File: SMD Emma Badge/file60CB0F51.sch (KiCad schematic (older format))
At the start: 10 parts, among them U401 74164, U402 74LS595, U403 74164, U404 74HC86, U405 74HC04

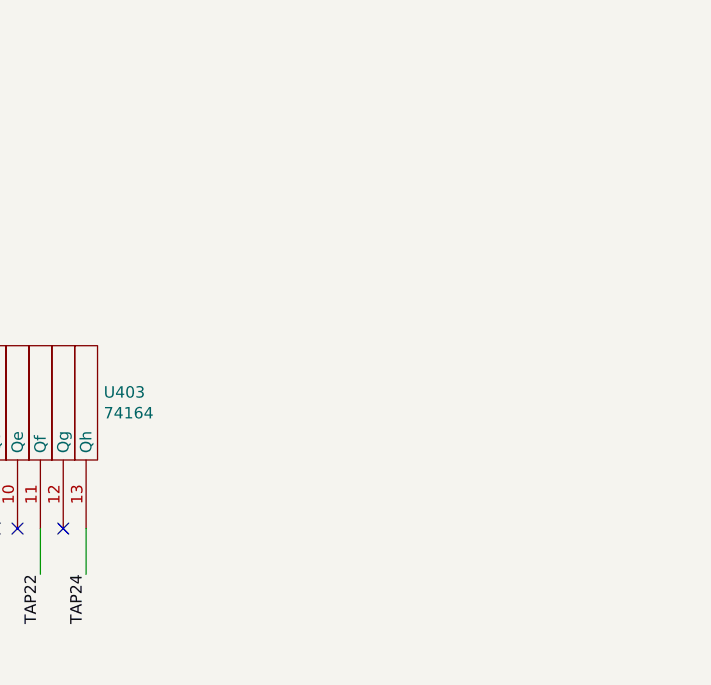
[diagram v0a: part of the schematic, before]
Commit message: Add power-on reset
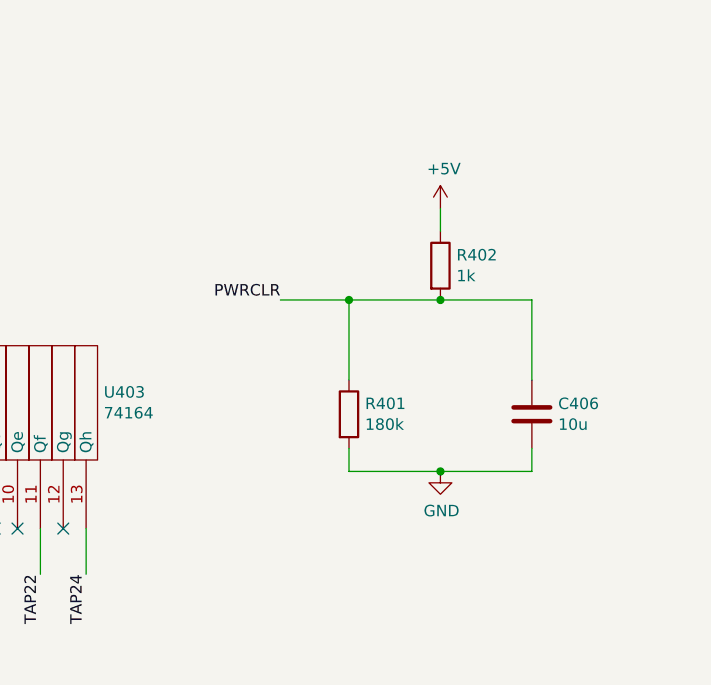
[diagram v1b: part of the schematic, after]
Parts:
- added C406: 10u, Capacitor_SMD:C_0603_1608Metric, symbol Device:C
- added R401: 180k, Resistor_SMD:R_0603_1608Metric, symbol Device:R
- added R402: 1k, Resistor_SMD:R_0603_1608Metric, symbol Device:R
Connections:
- net +5V: now also R402.1
- net GND: now also C406.2, R401.2
- net PWRCLR: now also C406.1, R401.1, R402.2
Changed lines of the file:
@@
 Connection ~ 2250 3200
 $Comp
-L power:+5V #PWR?
+L power:+5V #PWR0401
 U 1 1 60D3F3C4
 P 3150 6650
-F 0 "#PWR?" H 3150 6500 50  0001 C CNN
+F 0 "#PWR0401" H 3150 6500 50  0001 C CNN
 F 1 "+5V" V 3165 6778 50  0000 L CNN
 F 2 "" H 3150 6650 50  0001 C CNN
@@
 $EndComp
 $Comp
-L power:GND #PWR?
+L power:GND #PWR0402
 U 1 1 60D4000F
 P 3150 7650
-F 0 "#PWR?" H 3150 7400 50  0001 C CNN
+F 0 "#PWR0402" H 3150 7400 50  0001 C CNN
 F 1 "GND" V 3155 7522 50  0000 R CNN
 F 2 "" H 3150 7650 50  0001 C CNN
@@
 Connection ~ 3150 6650
 $Comp
-L power:GND #PWR?
+L power:GND #PWR0408
 U 1 1 60D48516
 P 10350 5900
-F 0 "#PWR?" H 10350 5650 50  0001 C CNN
+F 0 "#PWR0408" H 10350 5650 50  0001 C CNN
 F 1 "GND" H 10355 5727 50  0000 C CNN
 F 2 "" H 10350 5900 50  0001 C CNN
@@
 	10700 4650 10700 5100
 $Comp
-L power:+5V #PWR?
+L power:+5V #PWR0407
 U 1 1 60D50F40
 P 10250 4650
-F 0 "#PWR?" H 10250 4500 50  0001 C CNN
+F 0 "#PWR0407" H 10250 4500 50  0001 C CNN
 F 1 "+5V" H 10265 4823 50  0000 C CNN
 F 2 "" H 10250 4650 50  0001 C CNN
@@
 	10250 4650 10700 4650
 $Comp
-L power:+5V #PWR?
+L power:+5V #PWR0404
 U 1 1 60D51E1E
 P 7050 3100
-F 0 "#PWR?" H 7050 2950 50  0001 C CNN
+F 0 "#PWR0404" H 7050 2950 50  0001 C CNN
 F 1 "+5V" H 7065 3273 50  0000 C CNN
 F 2 "" H 7050 3100 50  0001 C CNN
@@
 $EndComp
 $Comp
-L power:GND #PWR?
+L power:GND #PWR0403
 U 1 1 60D52CD0
 P 7000 2450
-F 0 "#PWR?" H 7000 2200 50  0001 C CNN
+F 0 "#PWR0403" H 7000 2200 50  0001 C CNN
 F 1 "GND" H 7005 2277 50  0000 C CNN
 F 2 "" H 7000 2450 50  0001 C CNN
@@
 	6900 3100 6900 3000
 Connection ~ 7050 3100
+$Comp
+L power:+5V #PWR0405
+U 1 1 60C9A9B2
+P 9900 1900
+F 0 "#PWR0405" H 9900 1750 50  0001 C CNN
+F 1 "+5V" H 9915 2073 50  0000 C CNN
+F 2 "" H 9900 1900 50  0001 C CNN
+F 3 "" H 9900 1900 50  0001 C CNN
+	1    9900 1900
+	1    0    0    -1
+$EndComp
+$Comp
+L Device:R R?
+U 1 1 60C9A9B9
+P 9900 2150
+AR Path="/60B031D5/60C9A9B9" Ref="R?"  Part="1"
+AR Path="/60B094D9/60C9A9B9" Ref="R?"  Part="1"
+AR Path="/60B13096/60C9A9B9" Ref="R?"  Part="1"
+AR Path="/60CB0F52/60C9A9B9" Ref="R402"  Part="1"
+F 0 "R402" H 9970 2196 50  0000 L CNN
+F 1 "1k" H 9970 2105 50  0000 L CNN
+F 2 "Resistor_SMD:R_0603_1608Metric" V 9830 2150 50  0001 C CNN
+F 3 "~" H 9900 2150 50  0001 C CNN
+F 4 "C21190" H 9900 2150 50  0001 C CNN "LCSC"
+	1    9900 2150
+	1    0    0    -1
+$EndComp
+$Comp
+L Device:R R?
+U 1 1 60C9A9C0
+P 9500 2800
+AR Path="/60B031D5/60C9A9C0" Ref="R?"  Part="1"
+AR Path="/60B094D9/60C9A9C0" Ref="R?"  Part="1"
+AR Path="/60B13096/60C9A9C0" Ref="R?"  Part="1"
+AR Path="/60CB0F52/60C9A9C0" Ref="R401"  Part="1"
+F 0 "R401" H 9570 2846 50  0000 L CNN
+F 1 "180k" H 9570 2755 50  0000 L CNN
+F 2 "Resistor_SMD:R_0603_1608Metric" V 9430 2800 50  0001 C CNN
+F 3 "~" H 9500 2800 50  0001 C CNN
+F 4 "C22827" H 9500 2800 50  0001 C CNN "LCSC"
+	1    9500 2800
+	1    0    0    -1
+$EndComp
+$Comp
+L Device:C C?
+U 1 1 60C9A9C7
+P 10300 2800
+AR Path="/60B031D5/60C9A9C7" Ref="C?"  Part="1"
+AR Path="/60B094D9/60C9A9C7" Ref="C?"  Part="1"
+AR Path="/60B13096/60C9A9C7" Ref="C?"  Part="1"
+AR Path="/60CB0F52/60C9A9C7" Ref="C406"  Part="1"
+F 0 "C406" H 10415 2846 50  0000 L CNN
+F 1 "10u" H 10415 2755 50  0000 L CNN
+F 2 "Capacitor_SMD:C_0603_1608Metric" H 10338 2650 50  0001 C CNN
+F 3 "~" H 10300 2800 50  0001 C CNN
+F 4 " C19702" H 10300 2800 50  0001 C CNN "LCSC"
+	1    10300 2800
+	1    0    0    -1
+$EndComp
+$Comp
+L power:GND #PWR0406
+U 1 1 60C9A9CD
+P 9900 3050
+F 0 "#PWR0406" H 9900 2800 50  0001 C CNN
+F 1 "GND" H 9905 2877 50  0000 C CNN
+F 2 "" H 9900 3050 50  0001 C CNN
+F 3 "" H 9900 3050 50  0001 C CNN
+	1    9900 3050
+	1    0    0    -1
+$EndComp
+Wire Wire Line
+	9500 2950 9500 3050
+Wire Wire Line
+	9500 3050 9900 3050
+Wire Wire Line
+	9900 3050 10300 3050
+Wire Wire Line
+	10300 3050 10300 2950
+Connection ~ 9900 3050
+Wire Wire Line
+	9500 2650 9500 2300
+Wire Wire Line
+	9500 2300 9900 2300
+Wire Wire Line
+	10300 2650 10300 2300
+Wire Wire Line
+	10300 2300 9900 2300
+Connection ~ 9900 2300
+Wire Wire Line
+	9900 2000 9900 1900
+Text Label 9200 2300 2    50   ~ 0
+PWRCLR
+Wire Wire Line
+	9200 2300 9500 2300
+Connection ~ 9500 2300
 $EndSCHEMATC

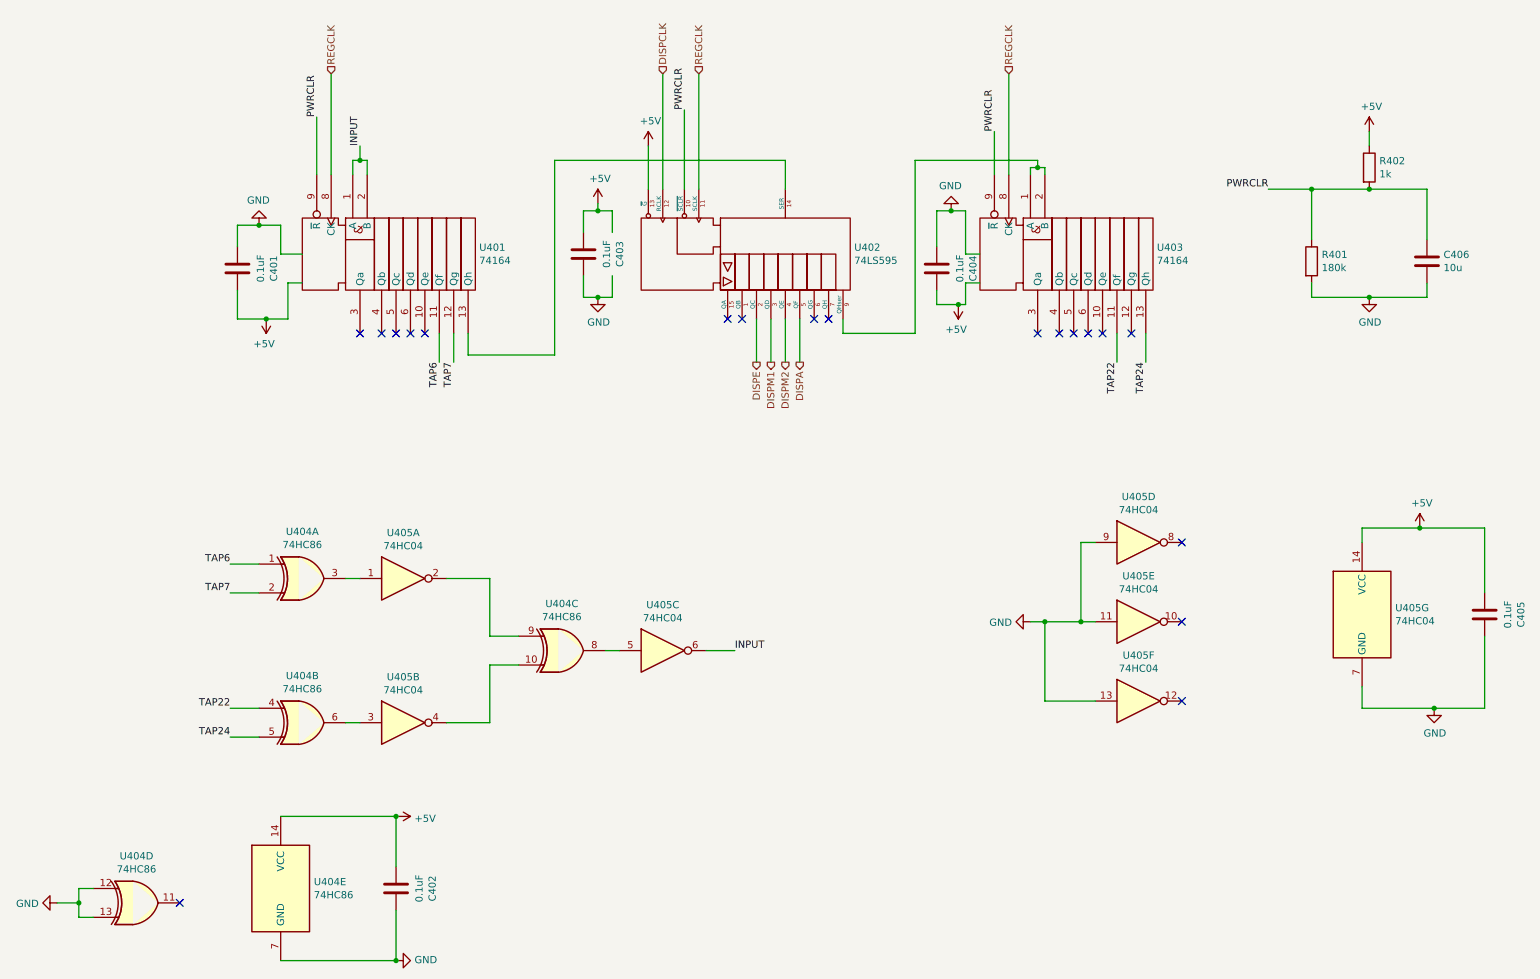
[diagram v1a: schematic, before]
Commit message: Routing the registers
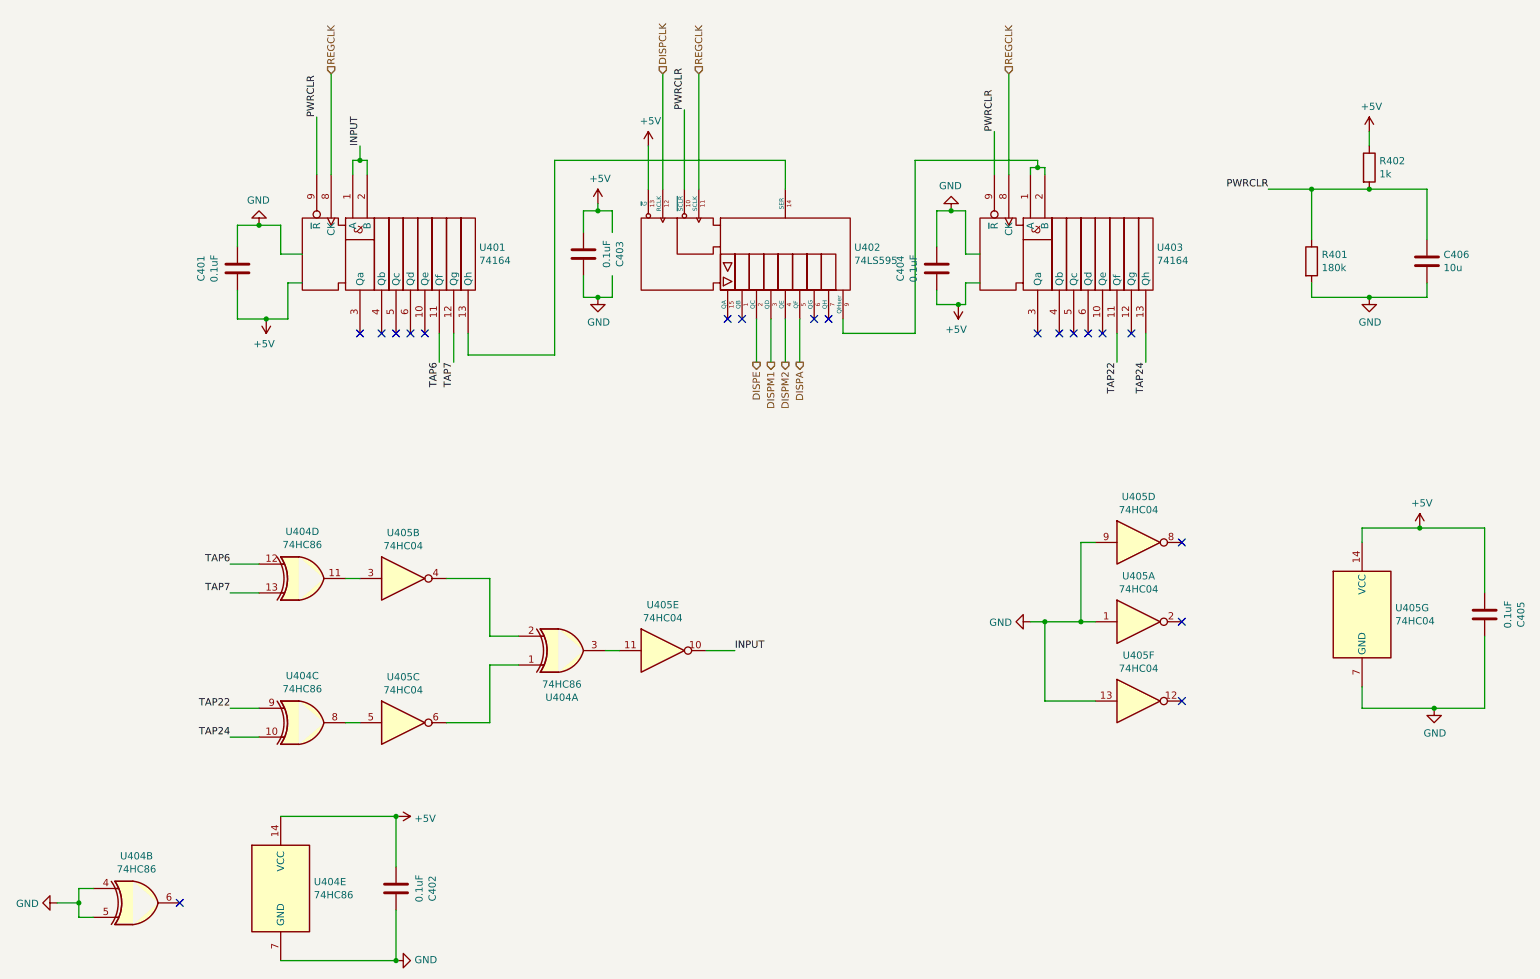
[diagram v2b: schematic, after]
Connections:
- net +5V: now also C401.2, C404.2; no longer C401.1, C404.1
- net GND: now also C401.1, C404.1, U404.4, U404.5, U405.1; no longer C401.2, C404.2, U404.12, U404.13, U405.11
- net INPUT: now also U405.10; no longer U405.6
- net TAP22: now also U404.9; no longer U404.4
- net TAP24: now also U404.10; no longer U404.5
- net TAP6: now also U404.12; no longer U404.1
- net TAP7: now also U404.13; no longer U404.2
- net at U404.3: now also U405.11; no longer U405.1
- net at U404.6: no longer U405.3
- net at U405.4: now also U404.2; no longer U404.10
- net at U405.2: no longer U404.9
- net at U404.11: now also U405.3
- new net: U404.1, U405.6
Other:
- moved on the sheet: U404A, U404B, U404C, U404D, U405A, U405B, U405C, U405E
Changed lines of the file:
@@
 L 74xx:74HC86 U404
 U 1 1 60CCCFC9
+P 4300 5500
+F 0 "U404" H 4300 5825 50  0000 C CNN
+F 1 "74HC86" H 4300 5734 50  0000 C CNN
+F 2 "" H 4300 5500 50  0001 C CNN
+F 3 "http://www.ti.com/lit/gpn/sn74HC86" H 4300 5500 50  0001 C CNN
+	1    4300 5500
+	1    0    0    1
+$EndComp
+$Comp
+L 74xx:74HC86 U404
+U 2 1 60CCEC7D
+P 1350 7250
+F 0 "U404" H 1350 7575 50  0000 C CNN
+F 1 "74HC86" H 1350 7484 50  0000 C CNN
+F 2 "" H 1350 7250 50  0001 C CNN
+F 3 "http://www.ti.com/lit/gpn/sn74HC86" H 1350 7250 50  0001 C CNN
+	2    1350 7250
+	1    0    0    -1
+$EndComp
+$Comp
+L 74xx:74HC86 U404
+U 3 1 60CD1561
+P 2500 6000
+F 0 "U404" H 2500 6325 50  0000 C CNN
+F 1 "74HC86" H 2500 6234 50  0000 C CNN
+F 2 "" H 2500 6000 50  0001 C CNN
+F 3 "http://www.ti.com/lit/gpn/sn74HC86" H 2500 6000 50  0001 C CNN
+	3    2500 6000
+	1    0    0    -1
+$EndComp
+$Comp
+L 74xx:74HC86 U404
+U 4 1 60CD320B
 P 2500 5000
 F 0 "U404" H 2500 5325 50  0000 C CNN
@@
 F 2 "" H 2500 5000 50  0001 C CNN
 F 3 "http://www.ti.com/lit/gpn/sn74HC86" H 2500 5000 50  0001 C CNN
-	1    2500 5000
-	1    0    0    -1
-$EndComp
-$Comp
-L 74xx:74HC86 U404
-U 2 1 60CCEC7D
-P 2500 6000
-F 0 "U404" H 2500 6325 50  0000 C CNN
-F 1 "74HC86" H 2500 6234 50  0000 C CNN
-F 2 "" H 2500 6000 50  0001 C CNN
-F 3 "http://www.ti.com/lit/gpn/sn74HC86" H 2500 6000 50  0001 C CNN
-	2    2500 6000
-	1    0    0    -1
-$EndComp
-$Comp
-L 74xx:74HC86 U404
-U 3 1 60CD1561
-P 4300 5500
-F 0 "U404" H 4300 5825 50  0000 C CNN
-F 1 "74HC86" H 4300 5734 50  0000 C CNN
-F 2 "" H 4300 5500 50  0001 C CNN
-F 3 "http://www.ti.com/lit/gpn/sn74HC86" H 4300 5500 50  0001 C CNN
-	3    4300 5500
-	1    0    0    -1
-$EndComp
-$Comp
-L 74xx:74HC86 U404
-U 4 1 60CD320B
-P 1350 7250
-F 0 "U404" H 1350 7575 50  0000 C CNN
-F 1 "74HC86" H 1350 7484 50  0000 C CNN
-F 2 "" H 1350 7250 50  0001 C CNN
-F 3 "http://www.ti.com/lit/gpn/sn74HC86" H 1350 7250 50  0001 C CNN
-	4    1350 7250
+	4    2500 5000
 	1    0    0    -1
 $EndComp
@@
 L 74xx:74HC04 U405
 U 1 1 60CD8C4F
+P 8300 5300
+F 0 "U405" H 8300 5617 50  0000 C CNN
+F 1 "74HC04" H 8300 5526 50  0000 C CNN
+F 2 "" H 8300 5300 50  0001 C CNN
+F 3 "https://assets.nexperia.com/documents/data-sheet/74HC_HCT04.pdf" H 8300 5300 50  0001 C CNN
+	1    8300 5300
+	1    0    0    -1
+$EndComp
+$Comp
+L 74xx:74HC04 U405
+U 2 1 60CD9E44
 P 3200 5000
 F 0 "U405" H 3200 5317 50  0000 C CNN
@@
 F 2 "" H 3200 5000 50  0001 C CNN
 F 3 "https://assets.nexperia.com/documents/data-sheet/74HC_HCT04.pdf" H 3200 5000 50  0001 C CNN
-	1    3200 5000
-	1    0    0    -1
-$EndComp
-$Comp
-L 74xx:74HC04 U405
-U 2 1 60CD9E44
+	2    3200 5000
+	1    0    0    -1
+$EndComp
+$Comp
+L 74xx:74HC04 U405
+U 3 1 60CDB507
 P 3200 6000
 F 0 "U405" H 3200 6317 50  0000 C CNN
@@
 F 2 "" H 3200 6000 50  0001 C CNN
 F 3 "https://assets.nexperia.com/documents/data-sheet/74HC_HCT04.pdf" H 3200 6000 50  0001 C CNN
-	2    3200 6000
-	1    0    0    -1
-$EndComp
-$Comp
-L 74xx:74HC04 U405
-U 3 1 60CDB507
-P 5000 5500
-F 0 "U405" H 5000 5817 50  0000 C CNN
-F 1 "74HC04" H 5000 5726 50  0000 C CNN
-F 2 "" H 5000 5500 50  0001 C CNN
-F 3 "https://assets.nexperia.com/documents/data-sheet/74HC_HCT04.pdf" H 5000 5500 50  0001 C CNN
-	3    5000 5500
+	3    3200 6000
 	1    0    0    -1
 $EndComp
@@
 L 74xx:74HC04 U405
 U 5 1 60CDEE27
-P 8300 5300
-F 0 "U405" H 8300 5617 50  0000 C CNN
-F 1 "74HC04" H 8300 5526 50  0000 C CNN
-F 2 "" H 8300 5300 50  0001 C CNN
-F 3 "https://assets.nexperia.com/documents/data-sheet/74HC_HCT04.pdf" H 8300 5300 50  0001 C CNN
-	5    8300 5300
+P 5000 5500
+F 0 "U405" H 5000 5817 50  0000 C CNN
+F 1 "74HC04" H 5000 5726 50  0000 C CNN
+F 2 "" H 5000 5500 50  0001 C CNN
+F 3 "https://assets.nexperia.com/documents/data-sheet/74HC_HCT04.pdf" H 5000 5500 50  0001 C CNN
+	5    5000 5500
 	1    0    0    -1
 $EndComp
@@
 F 4 " C14663" V 2050 2850 50  0001 C CNN "LCSC"
 	1    2050 2850
-	-1   0    0    1
+	1    0    0    -1
 $EndComp
 $Comp
@@
 F 4 " C14663" V 6900 2850 50  0001 C CNN "LCSC"
 	1    6900 2850
-	-1   0    0    1
-$EndComp
-Wire Wire Line
+	1    0    0    -1
+$EndComp
+Wire Wire Line
